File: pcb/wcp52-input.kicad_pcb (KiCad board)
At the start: 4 copper layers, 0 parts

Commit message: Routed PCB
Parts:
- added C10: 1n, IPC7351-Nominal:CAPC1005X55, F.Cu at (123.0, 85.0)
- added C11: 1n, IPC7351-Nominal:CAPC1005X55, F.Cu at (127.0, 85.0)
- added C12: 680n, IPC7351-Nominal:CAPC2012X70, F.Cu at (121.0, 80.5)
- added C13: 47u, IPC7351-Nominal:CAPC3216X70, F.Cu at (121.5, 82.5)
- added C14: 330n, IPC7351-Nominal:CAPC1608X55, F.Cu at (116.2, 85.8)
- added C15: 220p, IPC7351-Nominal:CAPC1608X55, F.Cu at (118.0, 77.5)
- added C16: 10n, IPC7351-Nominal:CAPC1005X55, F.Cu at (101.5, 72.8)
- added C17: 22p 1%, IPC7351-Nominal:CAPC1608X55, F.Cu at (102.8, 83.0)
- added C18: 33p 1%, IPC7351-Nominal:CAPC1608X55, F.Cu at (105.0, 83.0)
- added C19: 22p 1%, IPC7351-Nominal:CAPC1608X55, F.Cu at (107.2, 83.0)
- added C2: 47u, IPC7351-Nominal:CAPC3216X70, F.Cu at (101.5, 65.5)
- added C3: 1n, IPC7351-Nominal:CAPC1005X55, F.Cu at (119.5, 68.0)
- added C4: 1n, IPC7351-Nominal:CAPC1005X55, F.Cu at (119.5, 65.0)
- added C5: 10n, IPC7351-Nominal:CAPC1005X55, F.Cu at (112.8, 78.8)
- added C6: 680n, IPC7351-Nominal:CAPC2012X70, F.Cu at (112.8, 80.2)
- added C7: 10n, IPC7351-Nominal:CAPC1005X55, F.Cu at (112.8, 84.2)
- added C8: 680n, IPC7351-Nominal:CAPC2012X70, F.Cu at (112.8, 82.8)
- added C9: 10n, IPC7351-Nominal:CAPC1005X55, F.Cu at (119.5, 79.0)
- added DZ1: ESD9L5.0ST5G, IPC-semi-nominal:SOD-923, F.Cu at (110.2, 66.8)
- added DZ2: ESD9L5.0ST5G, IPC-semi-nominal:SOD-923, F.Cu at (110.2, 64.2)
- added DZ3: BZX84C2V7, IPC-semi-nominal:SOT-23, B.Cu at (110.0, 69.0)
- added DZ4: BZX84C2V7, IPC-semi-nominal:SOT-23, B.Cu at (110.0, 65.0)
- added DZ5: ESD9L5.0ST5G, IPC-semi-nominal:SOD-923, F.Cu at (120.0, 75.5)
- added DZ6: ESD9L5.0ST5G, IPC-semi-nominal:SOD-923, F.Cu at (120.0, 73.0)
- added DZ7: BZX84C2V7, IPC-semi-nominal:SOT-23, B.Cu at (120.0, 76.0)
- added DZ8: BZX84C2V7, IPC-semi-nominal:SOT-23, B.Cu at (120.0, 72.0)
- added E1: 600, IPC7351-Nominal:INDC1005X60, B.Cu at (95.0, 80.0)
- added E2: 600, IPC7351-Nominal:INDC1005X60, B.Cu at (96.0, 70.0)
- added F1: 50mA, IPC7351-Nominal:RESC1005X40, F.Cu at (108.2, 65.5)
- added F2: 50mA, IPC7351-Nominal:RESC1005X40, F.Cu at (121.5, 74.2)
- added J1: 5V, conn:CONN_3-SIL, F.Cu at (92.0, 75.0)
- added J3: IN1, conn:CONN-2_CONSMA001-SMD-G, F.Cu at (92.0, 65.0)
- added J4: IN2, conn:CONN-2_CONSMA001-SMD-G, F.Cu at (131.0, 70.5)
- added J5: CTRL, conn:CONN_2-SIL, F.Cu at (131.0, 61.0)
- added J6: PHASEREF, conn:CONN-2_CONSMA001-SMD-G, F.Cu at (92.0, 84.0)
- added J7: 5V, conn:CONN_2-SIL, F.Cu at (131.0, 80.0)
- added L1: 27n 2%, IPC7351-Nominal:INDC1005X60, F.Cu at (103.8, 81.0)
- added L2: 27n 2%, IPC7351-Nominal:INDC1005X60, F.Cu at (106.2, 81.0)
- added Q1: PMV160UP, IPC-semi-nominal:SOT-23, B.Cu at (91.0, 79.0)
- added Q2: 2N7002, IPC-semi-nominal:SOT-23, B.Cu at (93.0, 71.0)
- added Q3: MMBT3906, IPC-semi-nominal:SOT-23, F.Cu at (114.0, 58.0)
- added Q4: 2N7002, IPC-semi-nominal:SOT-23, F.Cu at (118.0, 58.0)
- added Q5: 2N7002, IPC-semi-nominal:SOT-23, F.Cu at (124.0, 58.0)
- added Q6: MMBT3904, IPC-semi-nominal:SOT-23, F.Cu at (105.0, 68.5)
- added Q7: BFR540, IPC-semi-nominal:SOT-23, F.Cu at (105.0, 77.0)
- added Q8: BFR540, IPC-semi-nominal:SOT-23, F.Cu at (105.0, 72.5)
- added R1: 1k6 1%, IPC7351-Nominal:RESC1005X40, F.Cu at (106.5, 63.8)
- added R10: 1k, IPC7351-Nominal:RESC1005X40, B.Cu at (120.0, 69.5)
- added R11: 1k, IPC7351-Nominal:RESC1005X40, F.Cu at (111.0, 58.0)
- added R12: 10k, IPC7351-Nominal:RESC1005X40, F.Cu at (121.0, 57.0)
- added R13: 220, IPC7351-Nominal:RESC1005X40, F.Cu at (121.2, 67.2)
- added R14: 220, IPC7351-Nominal:RESC1005X40, F.Cu at (121.2, 65.8)
- added R15: 10k, IPC7351-Nominal:RESC1005X40, F.Cu at (123.0, 68.0)
- added R16: 10k, IPC7351-Nominal:RESC1005X40, F.Cu at (123.0, 65.0)
- added R17: 2k2, IPC7351-Nominal:RESC1005X40, F.Cu at (109.2, 81.5)
- added R18: 53r6, IPC7351-Nominal:RESC1005X40, F.Cu at (110.5, 81.5)
- added R19: 49r9, IPC7351-Nominal:RESC1005X40, F.Cu at (120.8, 84.2)
- added R2: 1k6 1%, IPC7351-Nominal:RESC1005X40, F.Cu at (105.0, 65.2)
- added R20: 200, IPC7351-Nominal:RESC1005X40, F.Cu at (107.8, 74.5)
- added R21: 200, IPC7351-Nominal:RESC1005X40, F.Cu at (109.0, 74.5)
- added R22: 200, IPC7351-Nominal:RESC1005X40, F.Cu at (107.8, 77.0)
- added R23: 1k, IPC7351-Nominal:RESC1005X40, F.Cu at (101.5, 74.0)
- added R24: 200, IPC7351-Nominal:RESC1005X40, F.Cu at (109.0, 77.0)
- added R25: 22, IPC7351-Nominal:RESC1005X40, F.Cu at (101.5, 71.5)
- added R26: 100, IPC7351-Nominal:RESC1005X40, F.Cu at (101.0, 78.0)
- added R27: 100, IPC7351-Nominal:RESC1005X40, F.Cu at (101.5, 79.5)
- added R28: 100, IPC7351-Nominal:RESC1005X40, F.Cu at (102.5, 78.0)
- added R3: 1k, IPC7351-Nominal:RESC1005X40, B.Cu at (110.0, 72.0)
- added R4: 1k, IPC7351-Nominal:RESC1005X40, B.Cu at (107.0, 66.5)
- added R5: 49r9, IPC7351-Nominal:RESC1005X40, F.Cu at (119.0, 85.5)
- added R6: 49r9, IPC7351-Nominal:RESC1005X40, F.Cu at (129.0, 84.5)
- added R7: 1k6 1%, IPC7351-Nominal:RESC1005X40, F.Cu at (123.0, 73.0)
- added R8: 1k6 1%, IPC7351-Nominal:RESC1005X40, F.Cu at (123.0, 75.5)
- added R9: 1k, IPC7351-Nominal:RESC1005X40, B.Cu at (120.0, 79.0)
- added U1: MASWSS0162, IPC7351-Nominal:SOIC127P600X175-8, F.Cu at (115.0, 66.5)
- added U2: MASWSS0162, IPC7351-Nominal:SOIC127P600X175-8, F.Cu at (115.0, 72.5)
- added U3: AD8310, IPC7351-Nominal:SOP65P490X109-8, F.Cu at (117.0, 81.5)
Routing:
- net GND: track 0.00 -> 311.3 mm, vias 0 -> 126
- net /Switching/CTRL: track 0.00 -> 31.9 mm
- net /Buffer_Filter/IN: track 0.00 -> 27.0 mm
- net -5: track 0.00 -> 25.3 mm, vias 0 -> 6
- net Net-(Q4-Pad3): track 0.00 -> 22.2 mm, vias 0 -> 3
- net /Protection/IN1: track 0.00 -> 18.1 mm, vias 0 -> 5
- net +5: track 0.00 -> 15.4 mm, vias 0 -> 5
- net /Protection/IN2: track 0.00 -> 15.2 mm, vias 0 -> 2
- net Net-(C4-Pad1): track 0.00 -> 14.0 mm, vias 0 -> 2
- net Net-(C3-Pad1): track 0.00 -> 13.9 mm, vias 0 -> 3
- net Net-(C10-Pad1): track 0.00 -> 12.5 mm, vias 0 -> 2
- net /Buffer_Filter/PHASEREF: track 0.00 -> 12.4 mm, vias 0 -> 3
- net Net-(Q5-Pad3): track 0.00 -> 11.2 mm, vias 0 -> 3
- net /Detector/4V6_FILTERED: track 0.00 -> 10.9 mm
- net Net-(DZ2-Pad2): track 0.00 -> 9.39 mm, vias 0 -> 2
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- added copper zone on In2.Cu, net +5
- added copper zone on In2.Cu, net -5
- added copper zone on F.Cu, net GND
- added copper zone on In1.Cu, net GND
- added copper zone on In2.Cu, net GND
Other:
- board outline added: 48.5 x 35 mm
- net class Default: clearance 0.2 -> 0.18
- rule trace_clearance: 0.2 -> 0.18

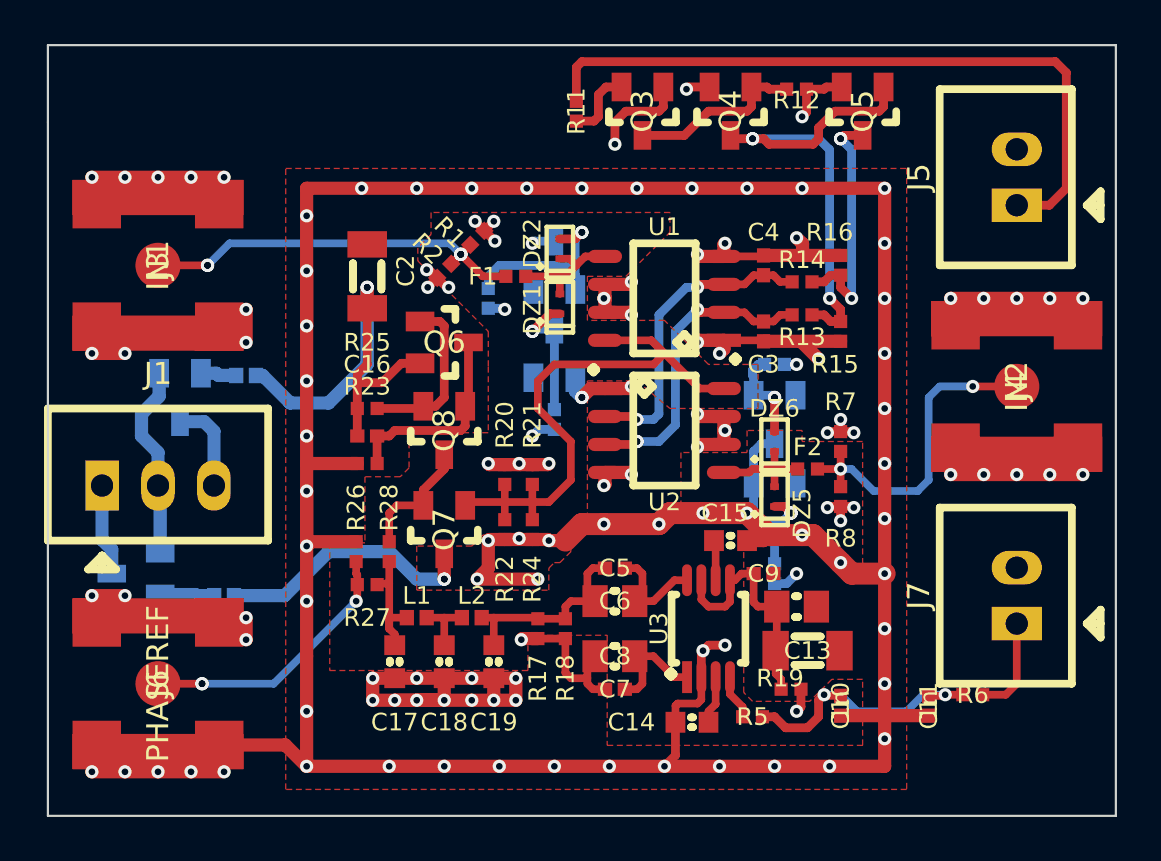
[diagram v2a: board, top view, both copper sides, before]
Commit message: Rearranged - smaller PCB
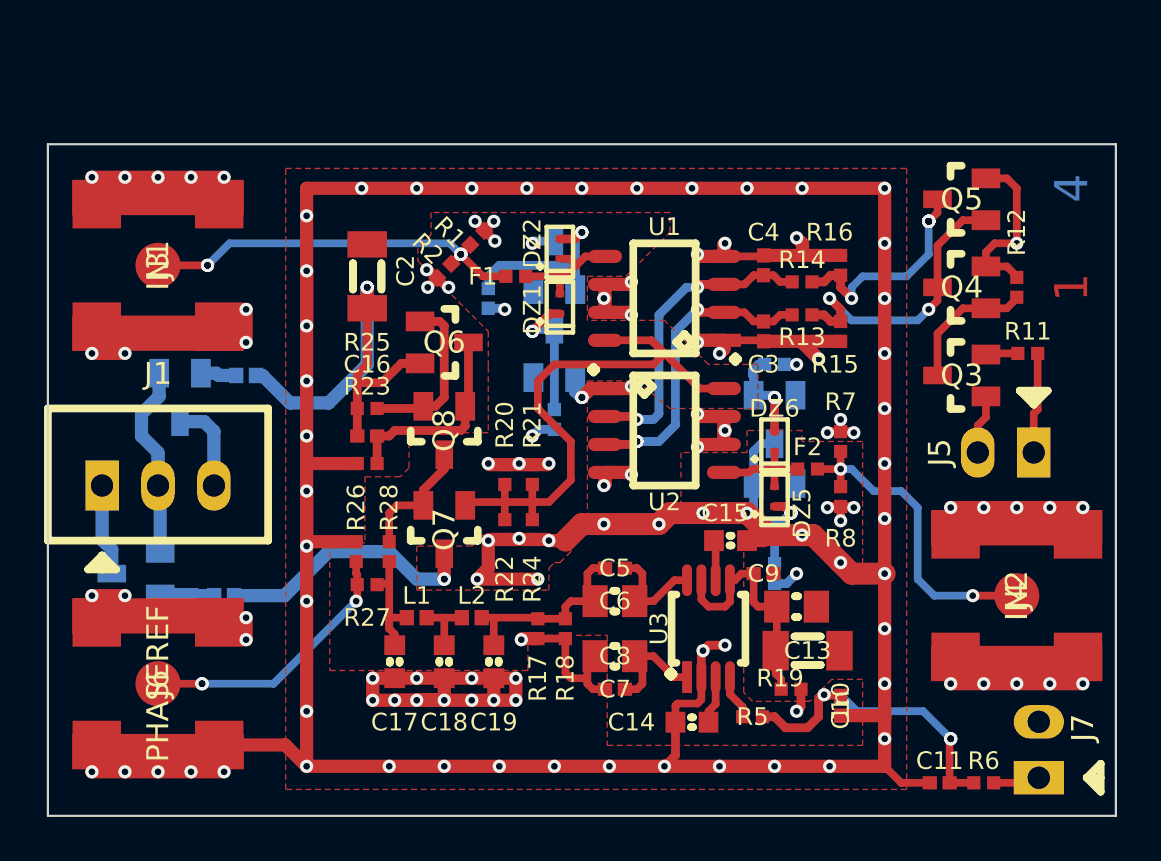
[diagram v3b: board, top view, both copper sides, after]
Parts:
- moved R11 23.3 mm to (131.5, 69.0), turned to 180 degrees
- moved Q3 18.8 mm to (128.5, 70.0), turned to 180 degrees
- moved R12 13.5 mm to (131.0, 66.0), turned to 90 degrees
- moved Q4 13.2 mm to (128.5, 66.0), turned to 180 degrees
- moved J5 12.5 mm to (130.5, 73.5), turned to 180 degrees
- moved J4 9.50 mm to (131.0, 80.0)
- moved J7 7.07 mm to (132.0, 87.0)
- moved Q5 6.02 mm to (128.5, 62.0), turned to 180 degrees
- moved R6 4.03 mm to (129.5, 88.5)
- moved C11 3.54 mm to (127.5, 88.5), turned to 180 degrees
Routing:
- net /Switching/CTRL: track 31.9 -> 4.57 mm
- net Net-(Q4-Pad3): track 22.2 -> 13.5 mm, vias 3 -> 2
- net -5: track 25.3 -> 29.2 mm, vias 6 -> 5
- net Net-(J7-Pad1): track 4.49 -> 2.15 mm
- net Net-(C10-Pad1): track 12.5 -> 14.6 mm, vias 2 -> 3
- net Net-(Q3-Pad3): track 8.03 -> 6.21 mm
- net Net-(Q3-Pad2): track 3.28 -> 1.47 mm
- net GND: track 311.3 -> 310.0 mm, vias 126 -> 125
- net Net-(Q5-Pad3): track 11.2 -> 9.97 mm, vias 3 -> 6
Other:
- board size 48.5 x 35 mm -> 48.5 x 30.5 mm
- board text added: "1"
- board text added: "2"
- board text added: "3"
- board text added: "4"

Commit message: PCB tweaks
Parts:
- moved C18 4.00 mm to (101.0, 83.0), turned to 180 degrees
- moved C19 3.05 mm to (104.8, 84.8)
- moved L2 2.83 mm to (104.2, 83.0)
- moved C17 2.30 mm to (101.0, 81.5), turned to 180 degrees
- moved L1 1.60 mm to (102.8, 82.2), turned to 90 degrees
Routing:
- net GND: track 310.0 -> 297.1 mm, vias 125 -> 119
- net /Detector/IN: track 9.37 -> 12.0 mm
- net Net-(C17-Pad1): track 5.77 -> 4.78 mm
- net /Buffer_Filter/IN: track 27.0 -> 26.3 mm
- net Net-(C18-Pad1): track 2.85 -> 2.35 mm
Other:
- board text added: "+5 0 -5"
- board text added: "2014-11"
- board text added: "WARNING: COVER TO RETAIN MAGIC"
- board text added: "WCP52 FRONTEND"
